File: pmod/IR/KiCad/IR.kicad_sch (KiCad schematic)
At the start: 8 parts, among them J1 Conn_02x06_Odd_Even, Q1 BC337, Q2 BC327

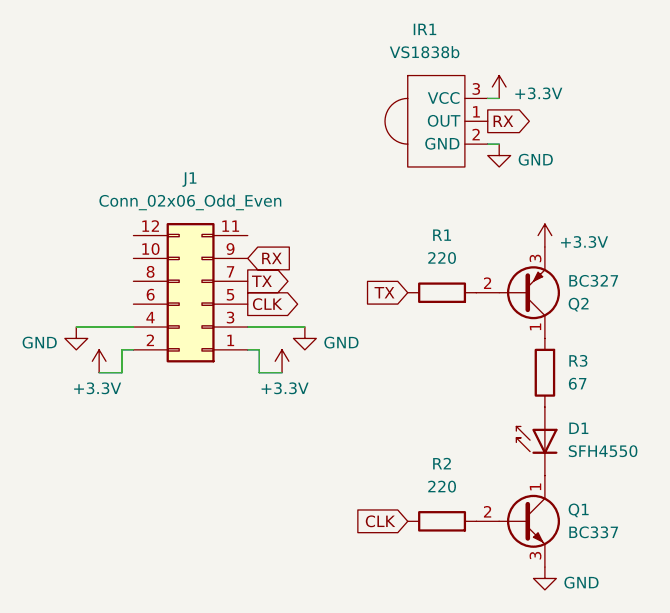
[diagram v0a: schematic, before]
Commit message: Update IR module
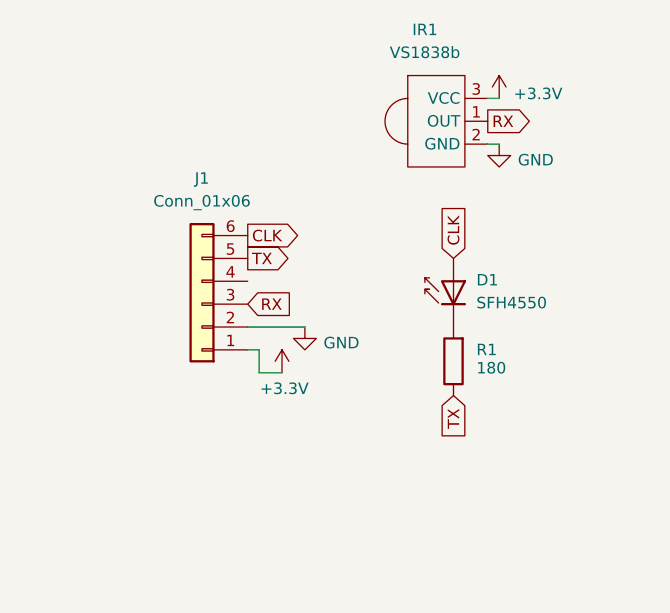
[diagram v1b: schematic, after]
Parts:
- removed J1: Conn_02x06_Odd_Even, Connector_PinHeader_2.54mm:PinHeader_2x06_P2.54mm_Horizontal, symbol Connector_Generic:Conn_02x06_Odd_Even
- removed Q1: BC337, Package_TO_SOT_THT:TO-92_Inline_Wide, symbol Transistor_BJT:BC337
- removed Q2: BC327, Package_TO_SOT_THT:TO-92_Inline_Wide, symbol Transistor_BJT:BC327
- removed R1, R2: 220, Resistor_THT:R_Axial_DIN0207_L6.3mm_D2.5mm_P2.54mm_Vertical, symbol Device:R
- added J1: Conn_01x06, Connector_PinHeader_2.54mm:PinHeader_1x06_P2.54mm_Horizontal, symbol Connector_Generic:Conn_01x06
- R1: renamed from R3; value 67 -> 180; footprint Resistor_THT:R_Axial_DIN0207_L6.3mm_D2.5mm_P2.54mm_Vertical -> Resistor_THT:R_Axial_DIN0207_L6.3mm_D2.5mm_P10.16mm_Horizontal
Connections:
- net +3.3V: now also J1.1 (Pin_1)
- net CLK: now also D1.2 (A), J1.6 (Pin_6)
- net GND: now also J1.2 (Pin_2)
- net RX: now also J1.3 (Pin_3)
- net TX: now also R1.1, J1.5 (Pin_5)
- net at D1.1 (K): now also R1.2
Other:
- moved on the sheet: D1, R1
